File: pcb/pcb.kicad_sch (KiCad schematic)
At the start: 35 parts, among them J1 GND, J10 SWDIO, J11 SWCLK, J12 USART2 TX, J13 USART2 RX, J14 VDD, J2 +3.6V, J3 LCD Data, J4 LCD RS, J5 LCD E, J6 3.3v, J7 ADC2, J8 GND, J9 USART1 TX, U1 TLV62569DBV, U2 STM32F446RETx

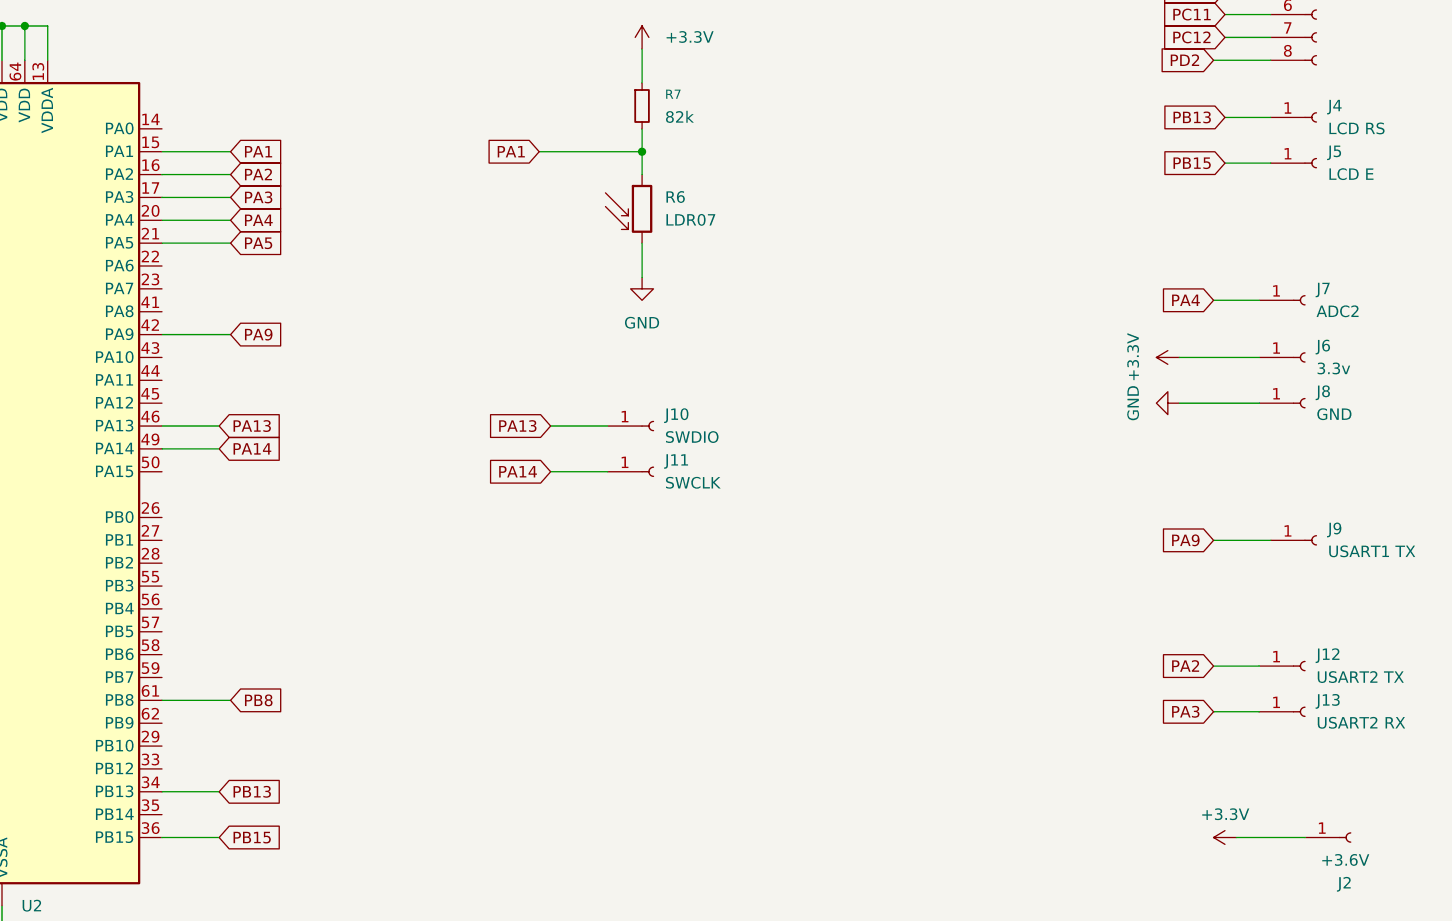
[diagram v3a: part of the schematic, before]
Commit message: better use of pins
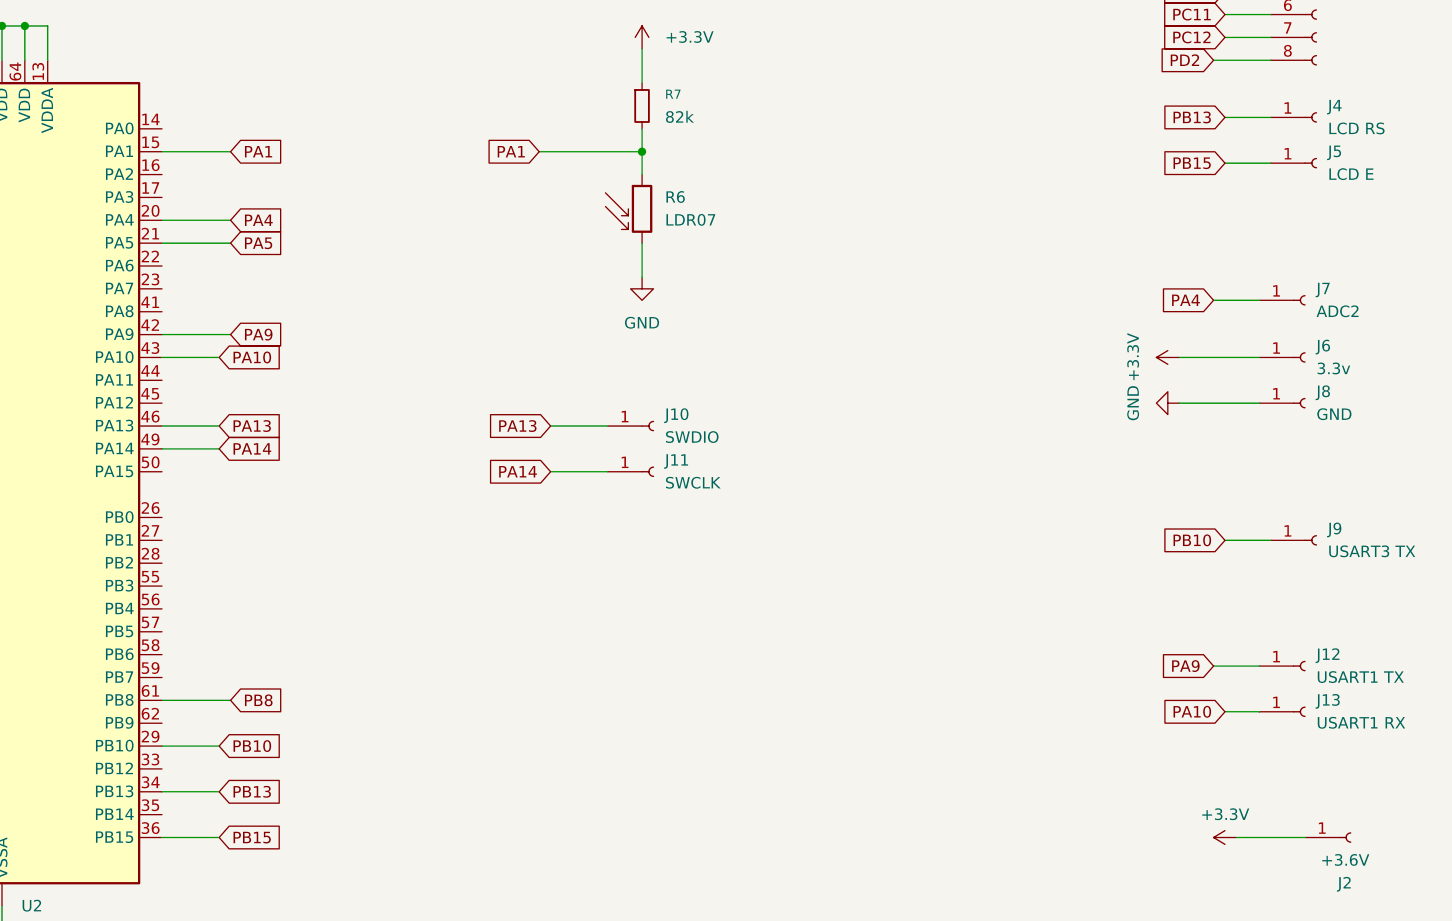
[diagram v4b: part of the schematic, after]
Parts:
- J12: value USART2 TX -> USART1 TX
- J13: value USART2 RX -> USART1 RX
- J9: value USART1 TX -> USART3 TX
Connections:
- net PA9: now also J12.1 (Pin_1); no longer J9.1 (Pin_1)
- net PB10: now reaches U2.29 (PB10)
- net PB10: now also J9.1 (Pin_1)
- net PA10: now reaches U2.43 (PA10)
- net PA10: now also J13.1 (Pin_1)
- net PA2: no longer names the net of U2.16 (PA2)
- net PA2: no longer J12.1 (Pin_1)
- net PA3: no longer names the net of U2.17 (PA3)
- net PA3: no longer J13.1 (Pin_1)
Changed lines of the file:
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@@
 	(wire
 		(pts
-			(xy 259.08 138.43) (xy 264.16 138.43)
+			(xy 129.54 67.31) (xy 129.54 71.12)
 		)
 		(stroke
@@
 	(wire
 		(pts
-			(xy 129.54 67.31) (xy 129.54 71.12)
+			(xy 104.14 25.4) (xy 104.14 29.21)
 		)
 		(stroke
@@
 	(wire
 		(pts
-			(xy 259.08 143.51) (xy 264.16 143.51)
+			(xy 121.92 67.31) (xy 121.92 71.12)
 		)
 		(stroke
@@
 	(wire
 		(pts
-			(xy 104.14 25.4) (xy 104.14 29.21)
+			(xy 121.92 67.31) (xy 124.46 67.31)
 		)
 		(stroke
@@
 	(wire
 		(pts
-			(xy 121.92 67.31) (xy 121.92 71.12)
+			(xy 142.24 147.32) (xy 148.59 147.32)
 		)
 		(stroke
@@
 	(wire
 		(pts
-			(xy 121.92 67.31) (xy 124.46 67.31)
+			(xy 121.92 62.23) (xy 121.92 67.31)
 		)
 		(stroke
@@
 	(wire
 		(pts
-			(xy 121.92 62.23) (xy 121.92 67.31)
+			(xy 260.35 143.51) (xy 264.16 143.51)
 		)
 		(stroke
@@
 	(wire
 		(pts
-			(xy 259.08 124.46) (xy 265.43 124.46)
+			(xy 260.35 124.46) (xy 265.43 124.46)
 		)
 		(stroke
@@
 	(wire
 		(pts
-			(xy 142.24 86.36) (xy 149.86 86.36)
-		)
-		(stroke
-			(width 0)
-			(type default)
-		)
-	)
-	(wire
-		(pts
 			(xy 191.77 111.76) (xy 185.42 111.76)
 		)
@@
 	(wire
 		(pts
+			(xy 259.08 138.43) (xy 264.16 138.43)
+		)
+		(stroke
+			(width 0)
+			(type default)
+		)
+	)
+	(wire
+		(pts
 			(xy 121.92 168.91) (xy 124.46 168.91)
 		)
@@
 	(wire
 		(pts
-			(xy 142.24 83.82) (xy 149.86 83.82)
-		)
-		(stroke
-			(width 0)
-			(type default)
-		)
-	)
-	(wire
-		(pts
 			(xy 96.52 144.78) (xy 101.6 144.78)
 		)
@@
 	(wire
 		(pts
+			(xy 142.24 104.14) (xy 148.59 104.14)
+		)
+		(stroke
+			(width 0)
+			(type default)
+		)
+	)
+	(wire
+		(pts
 			(xy 142.24 81.28) (xy 149.86 81.28)
 		)
@@
 		)
 	)
-	(global_label "PA13"
+	(global_label "PA10"
 		(shape input)
-		(at 185.42 111.76 180)
+		(at 260.35 143.51 180)
 		(fields_autoplaced yes)
 		(effects
@@
 		)
 		(property "Intersheetrefs" "${INTERSHEET_REFS}"
-			(at 177.6572 111.76 0)
+			(at 252.5872 143.51 0)
 			(effects
 				(font
@@
 		)
 	)
-	(global_label "PC10"
+	(global_label "PA13"
 		(shape input)
-		(at 260.35 63.5 180)
+		(at 185.42 111.76 180)
 		(fields_autoplaced yes)
 		(effects
@@
 		)
 		(property "Intersheetrefs" "${INTERSHEET_REFS}"
-			(at 252.4058 63.5 0)
+			(at 177.6572 111.76 0)
 			(effects
 				(font
@@
 		)
 	)
-	(global_label "PA4"
+	(global_label "PC10"
 		(shape input)
-		(at 259.08 97.79 180)
+		(at 260.35 63.5 180)
 		(fields_autoplaced yes)
 		(effects
@@
 		)
 		(property "Intersheetrefs" "${INTERSHEET_REFS}"
-			(at 252.5267 97.79 0)
+			(at 252.4058 63.5 0)
 			(effects
 				(font
@@
 		)
 	)
-	(global_label "PA14"
+	(global_label "PA4"
 		(shape input)
-		(at 185.42 116.84 180)
+		(at 259.08 97.79 180)
 		(fields_autoplaced yes)
 		(effects
@@
 		)
 		(property "Intersheetrefs" "${INTERSHEET_REFS}"
-			(at 177.6572 116.84 0)
+			(at 252.5267 97.79 0)
 			(effects
 				(font
@@
 		)
 	)
-	(global_label "PC9"
+	(global_label "PA14"
 		(shape input)
-		(at 92.71 124.46 180)
+		(at 185.42 116.84 180)
 		(fields_autoplaced yes)
 		(effects
@@
 		)
 		(property "Intersheetrefs" "${INTERSHEET_REFS}"
-			(at 85.9753 124.46 0)
+			(at 177.6572 116.84 0)
 			(effects
 				(font
@@
 		)
 	)
-	(global_label "PA2"
+	(global_label "PC9"
 		(shape input)
-		(at 259.08 138.43 180)
+		(at 92.71 124.46 180)
 		(fields_autoplaced yes)
 		(effects
@@
 		)
 		(property "Intersheetrefs" "${INTERSHEET_REFS}"
-			(at 252.5267 138.43 0)
+			(at 85.9753 124.46 0)
 			(effects
 				(font
@@
 		)
 	)
-	(global_label "PA1"
+	(global_label "PB10"
 		(shape input)
-		(at 184.15 81.28 180)
+		(at 260.35 124.46 180)
 		(fields_autoplaced yes)
 		(effects
@@
 		)
 		(property "Intersheetrefs" "${INTERSHEET_REFS}"
-			(at 177.5967 81.28 0)
+			(at 252.4058 124.46 0)
 			(effects
 				(font
@@
 		)
 	)
-	(global_label "PB8"
+	(global_label "PA1"
 		(shape input)
-		(at 259.08 58.42 180)
+		(at 184.15 81.28 180)
 		(fields_autoplaced yes)
 		(effects
@@
 		)
 		(property "Intersheetrefs" "${INTERSHEET_REFS}"
-			(at 252.3453 58.42 0)
+			(at 177.5967 81.28 0)
 			(effects
 				(font
@@
 		)
 	)
-	(global_label "PA3"
+	(global_label "PB8"
 		(shape input)
-		(at 259.08 143.51 180)
+		(at 259.08 58.42 180)
 		(fields_autoplaced yes)
 		(effects
@@
 		)
 		(property "Intersheetrefs" "${INTERSHEET_REFS}"
-			(at 252.5267 143.51 0)
+			(at 252.3453 58.42 0)
 			(effects
 				(font
@@
 	(global_label "PA9"
 		(shape input)
-		(at 259.08 124.46 180)
+		(at 259.08 138.43 180)
 		(fields_autoplaced yes)
 		(effects
@@
 		)
 		(property "Intersheetrefs" "${INTERSHEET_REFS}"
-			(at 252.5267 124.46 0)
+			(at 252.5267 138.43 0)
 			(effects
 				(font
@@
 		)
 	)
-	(global_label "PA3"
-		(shape input)
-		(at 149.86 86.36 0)
-		(fields_autoplaced yes)
-		(effects
-			(font
-				(size 1.27 1.27)
-			)
-			(justify left)
-		)
-		(property "Intersheetrefs" "${INTERSHEET_REFS}"
-			(at 156.4133 86.36 0)
-			(effects
-				(font
-					(size 1.27 1.27)
-				)
-				(justify left)
-				(hide yes)
-			)
-		)
-	)
-	(global_label "PA2"
+	(global_label "PD2"
 		(shape input)
-		(at 149.86 83.82 0)
+		(at 259.08 71.12 180)
 		(fields_autoplaced yes)
 		(effects
@@
 				(size 1.27 1.27)
 			)
-			(justify left)
+			(justify right)
 		)
 		(property "Intersheetrefs" "${INTERSHEET_REFS}"
-			(at 156.4133 83.82 0)
+			(at 252.3453 71.12 0)
 			(effects
 				(font
 					(size 1.27 1.27)
 				)
-				(justify left)
+				(justify right)
 				(hide yes)
 			)
 		)
 	)
-	(global_label "PD2"
+	(global_label "PC9"
 		(shape input)
-		(at 259.08 71.12 180)
+		(at 259.08 53.34 180)
 		(fields_autoplaced yes)
 		(effects
@@
 		)
 		(property "Intersheetrefs" "${INTERSHEET_REFS}"
-			(at 252.3453 71.12 0)
+			(at 252.3453 53.34 0)
 			(effects
 				(font
@@
 		)
 	)
-	(global_label "PC9"
+	(global_label "PC11"
 		(shape input)
-		(at 259.08 53.34 180)
+		(at 93.98 129.54 180)
 		(fields_autoplaced yes)
 		(effects
@@
 		)
 		(property "Intersheetrefs" "${INTERSHEET_REFS}"
-			(at 252.3453 53.34 0)
+			(at 86.0358 129.54 0)
 			(effects
 				(font
@@
 	(global_label "PC11"
 		(shape input)
-		(at 93.98 129.54 180)
+		(at 260.35 66.04 180)
 		(fields_autoplaced yes)
 		(effects
@@
 		)
 		(property "Intersheetrefs" "${INTERSHEET_REFS}"
-			(at 86.0358 129.54 0)
+			(at 252.4058 66.04 0)
 			(effects
 				(font
@@
 		)
 	)
-	(global_label "PC11"
+	(global_label "PB10"
 		(shape input)
-		(at 260.35 66.04 180)
+		(at 148.59 147.32 0)
 		(fields_autoplaced yes)
 		(effects
@@
 				(size 1.27 1.27)
 			)
-			(justify right)
+			(justify left)
 		)
 		(property "Intersheetrefs" "${INTERSHEET_REFS}"
-			(at 252.4058 66.04 0)
+			(at 156.5342 147.32 0)
 			(effects
 				(font
 					(size 1.27 1.27)
 				)
-				(justify right)
+				(justify left)
 				(hide yes)
 			)
@@
 		)
 	)
+	(global_label "PA10"
+		(shape input)
+		(at 148.59 104.14 0)
+		(fields_autoplaced yes)
+		(effects
+			(font
+				(size 1.27 1.27)
+			)
+			(justify left)
+		)
+		(property "Intersheetrefs" "${INTERSHEET_REFS}"
+			(at 156.3528 104.14 0)
+			(effects
+				(font
+					(size 1.27 1.27)
+				)
+				(justify left)
+				(hide yes)
+			)
+		)
+	)
 	(symbol
 		(lib_id "Connector:Conn_01x01_Socket")
@@
 			)
 		)
-		(property "Value" "USART2 TX"
+		(property "Value" "USART1 TX"
 			(at 270.51 139.6999 0)
 			(effects
@@
 			)
 		)
-		(property "Value" "USART2 RX"
+		(property "Value" "USART1 RX"
 			(at 270.51 144.7799 0)
 			(effects
@@
 			)
 		)
-		(property "Value" "USART1 TX"
+		(property "Value" "USART3 TX"
 			(at 271.78 125.7299 0)
 			(effects

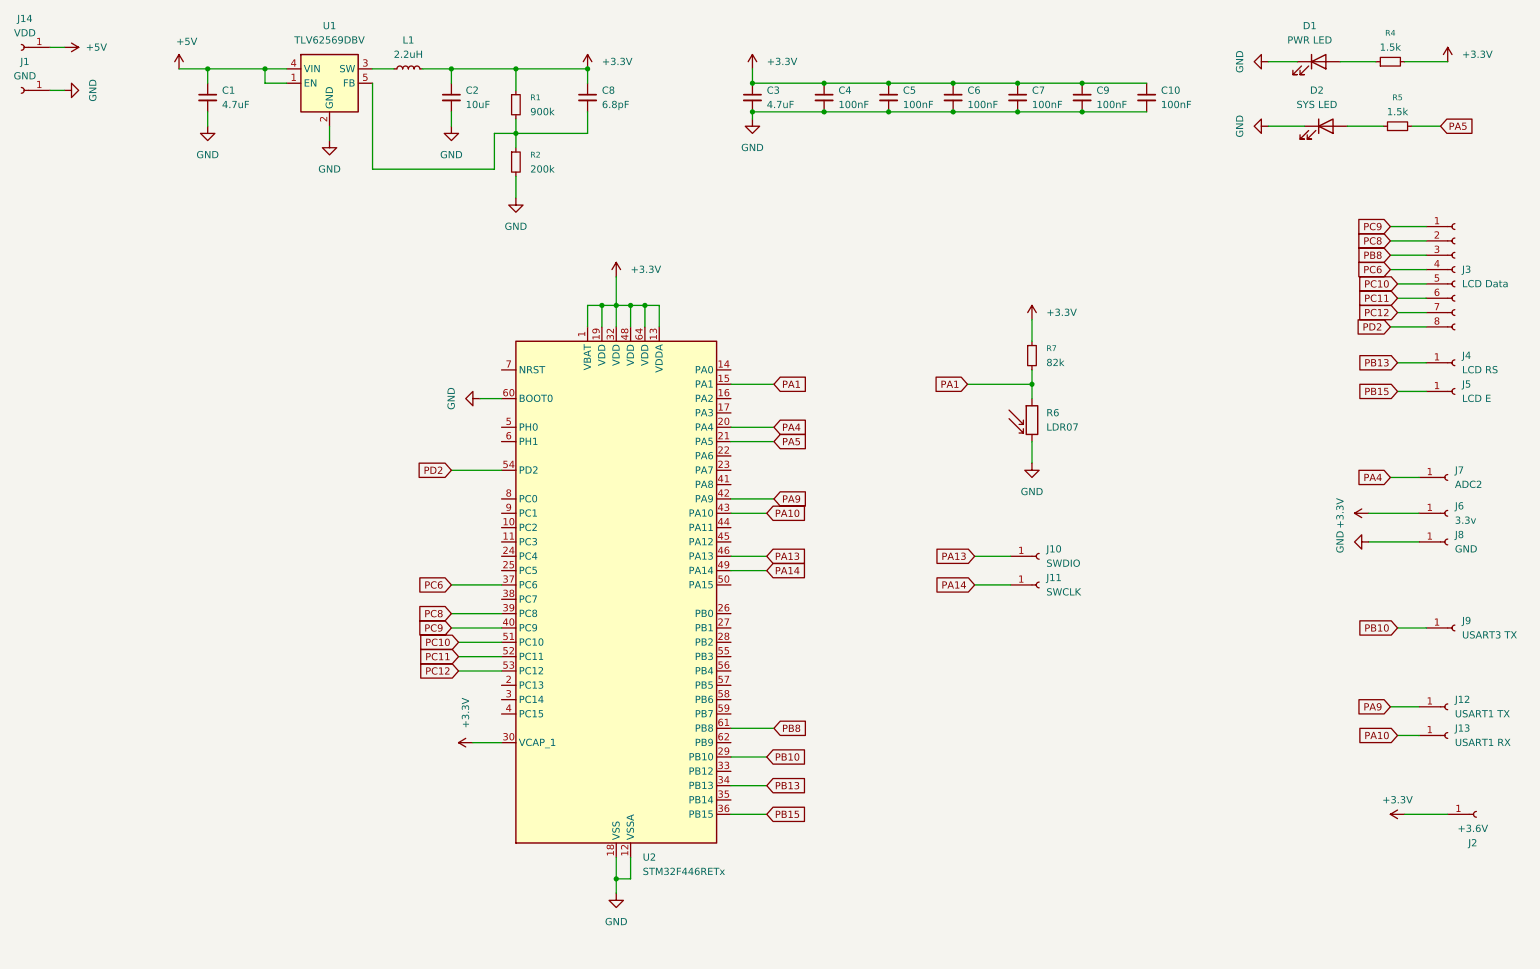
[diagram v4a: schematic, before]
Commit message: add battery charging circuit
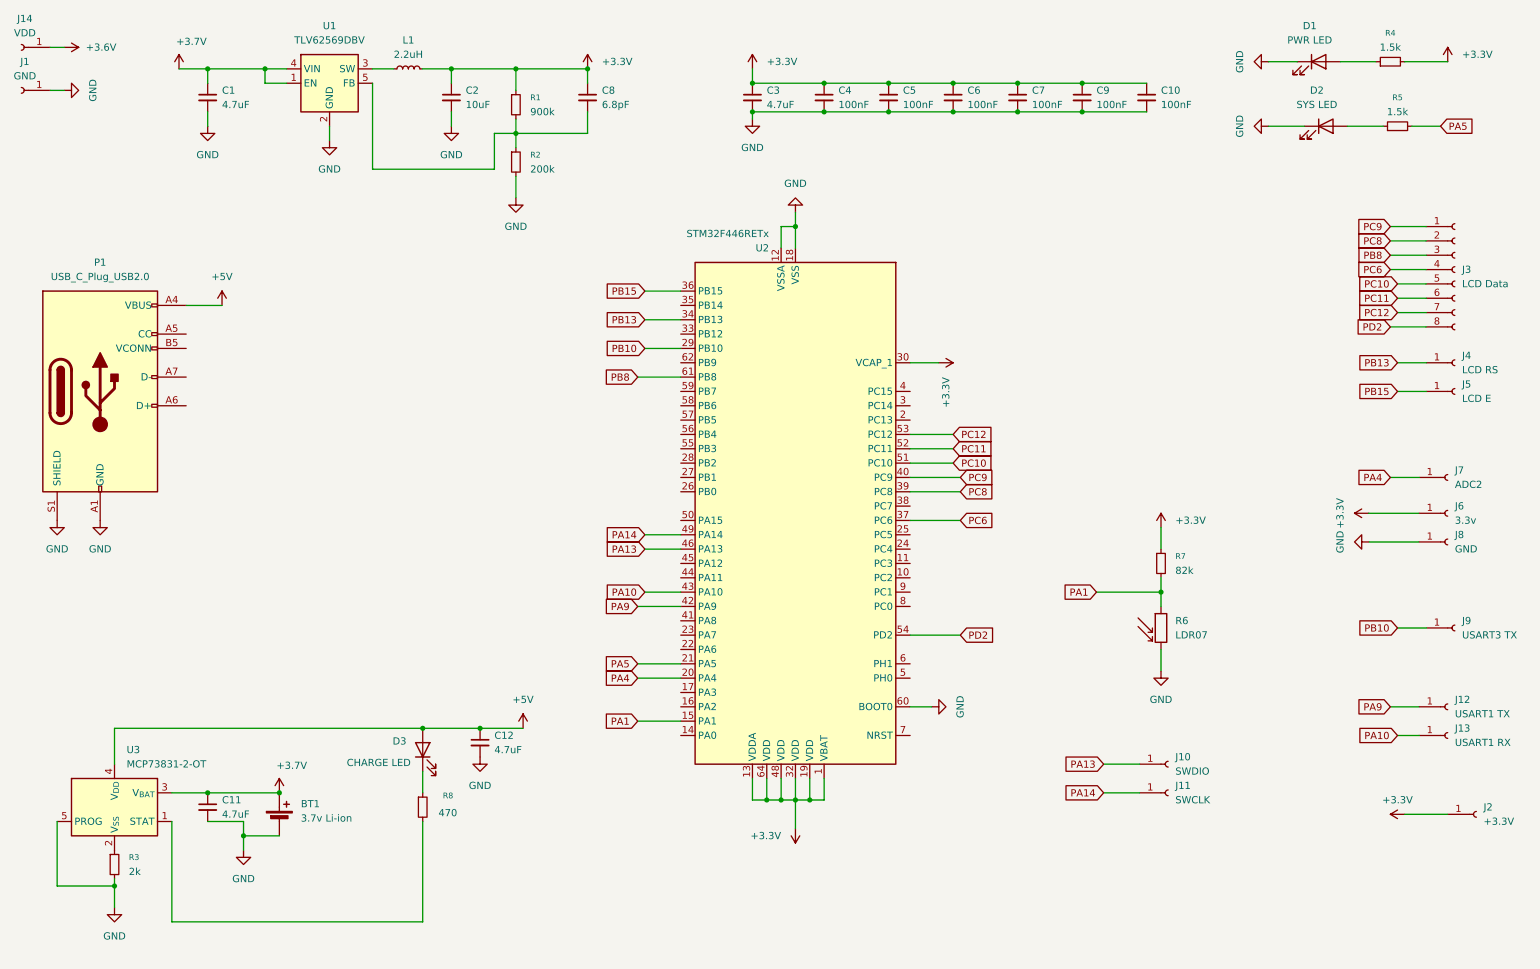
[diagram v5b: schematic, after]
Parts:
- added BT1: 3.7v Li-ion, symbol Device:Battery_Cell
- added C11, C12: 4.7uF, symbol Device:C_Small
- added D3: CHARGE LED, symbol Device:LED
- added P1: USB_C_Plug_USB2.0, symbol Connector:USB_C_Plug_USB2.0
- added R3: 2k, symbol Device:R_Small
- added R8: 470, symbol Device:R_Small
- added U3: MCP73831-2-OT, Package_TO_SOT_SMD:SOT-23-5, symbol Battery_Management:MCP73831-2-OT
- J2: value +3.6V -> +3.3V
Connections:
- net +5V: now also C12.1, D3.2 (A), P1.A4 (VBUS), P1.A9 (VBUS), P1.B4 (VBUS), P1.B9 (VBUS), U3.4 (V_{DD}); no longer C1.1, J14.1 (Pin_1), U1.1 (EN), U1.4 (VIN)
- net GND: now also BT1.2 (-), C11.2, C12.2, P1.A1 (GND), P1.A12 (GND), P1.B1 (GND), P1.B12 (GND), P1.S1 (SHIELD), R3.2, U3.5 (PROG)
- new net: R3.1, U3.2 (V_{SS})
- new net: R8.2, U3.1 (STAT)
- new net: D3.1 (K), R8.1
- new net +3.6V: J14.1 (Pin_1)
- new net +3.7V: BT1.1 (+), C1.1, C11.1, U1.1 (EN), U1.4 (VIN), U3.3 (V_{BAT})
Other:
- moved on the sheet: J10, J11, R6, R7, U2
